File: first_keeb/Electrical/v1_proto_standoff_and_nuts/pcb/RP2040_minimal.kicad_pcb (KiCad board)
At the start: 4 copper layers, 67.1 x 66.8 mm, 68 parts, among them P1 USB-TYPE-C-016, Q1 SN74LV1T34DBV, SW1 SKRKAHE020, SW2 BUTT0, SW3 BUTT1, U1 NCP1117-3.3_SOT223, U2 MCP1525-TT, U3 PRTR5V0U2X, U4 MCP6004, U5 STM32F401RCTx, Y1 16MHz

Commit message: stm32 pcb almost done
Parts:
- removed the C1 at (115.5, 76.1)
- removed the C2 at (108.3, 80.8)
- removed the R3 at (80.3, 97.1)
- removed the R8 at (138.9, 103.1)
- removed the U4 at (105.1, 91.9)
- added C11: 10u, Capacitor_SMD:C_1206_3216Metric, F.Cu at (106.9, 112.4)
- added C12: 10u, Capacitor_SMD:C_1206_3216Metric, F.Cu at (109.8, 107.8)
- added C13: 100n, Capacitor_SMD:C_0402_1005Metric, F.Cu at (83.7, 85.5)
- added C6: 100n, Capacitor_SMD:C_0402_1005Metric, F.Cu at (97.6, 81.0)
- added D1: 1N4148WS, Diode_SMD:D_SOD-323, F.Cu at (102.1, 82.4)
- added FB1: GZ2012D601TF, Capacitor_SMD:C_0805_2012Metric, F.Cu at (80.5, 88.4)
- added J1: Conn_01x04_Socket, Connector_PinSocket_2.54mm:PinSocket_1x04_P2.54mm_Vertical, F.Cu at (85.3, 76.1)
- added J2: Conn_01x04_Socket, Connector_PinSocket_2.54mm:PinSocket_1x04_P2.54mm_Vertical, F.Cu at (84.3, 72.5)
- added R11: DNP, Resistor_SMD:R_0402_1005Metric, F.Cu at (113.9, 96.4)
- added R12: 0, Resistor_SMD:R_0402_1005Metric, F.Cu at (142.9, 101.4)
- added R13: 0, Resistor_SMD:R_0402_1005Metric, F.Cu at (142.9, 103.4)
- added R4: DNP, Capacitor_SMD:C_0603_1608Metric, F.Cu at (135.9, 87.5)
- added R6: DNP, Resistor_SMD:R_0402_1005Metric, F.Cu at (142.9, 95.4)
- added SW2: SKRKAHE020, Button_Switch_SMD:SW_Push_SPST_NO_Alps_SKRK, B.Cu at (89.5, 83.5)
- added SW4: BUTT3, Button_Switch_SMD:SW_Push_1P1T_NO_6x6mm_H9.5mm, B.Cu at (112.0, 120.0)
- added U5: MCP6001-OT, Package_TO_SOT_SMD:SOT-23-5, F.Cu at (146.9, 96.6)
- added U6: MCP6001-OT, Package_TO_SOT_SMD:SOT-23-5, F.Cu at (110.4, 94.0)
- C10: value 1u -> 10u; footprint Capacitor_SMD:C_0402_1005Metric -> Capacitor_SMD:C_1206_3216Metric
- C9: value 100n -> 10u; footprint Capacitor_SMD:C_0402_1005Metric -> Capacitor_SMD:C_1206_3216Metric
- R10, R7: value 0 -> DNP; footprint Capacitor_SMD:C_0603_1608Metric -> Resistor_SMD:R_0402_1005Metric
- R3: renamed from R6; moved to B.Cu
- R5: value 0 -> 10k; footprint Capacitor_SMD:C_0603_1608Metric -> Resistor_SMD:R_0402_1005Metric
- R9: value 0 -> DNP
- SW1: moved to B.Cu
- SW3: renamed from SW2; value BUTT0 -> BUTT1
- SW5: renamed from SW3; value BUTT1 -> BUTT2
- U1: value NCP1117-3.3_SOT223 -> AMS1117-2.5
- U2: value MCP1525-TT -> ME6208A44M3G
- moved D4 66.9 mm to (136.5, 77.5)
- moved C22 66.8 mm to (138.6, 77.8), turned to 90 degrees
- moved R5 41.1 mm to (98.7, 90.0), turned to 90 degrees
- moved C21 38.9 mm to (70.4, 61.0)
- moved D3 38.9 mm to (68.2, 61.0)
- moved U2 36.5 mm to (110.1, 110.9), turned to 180 degrees
- moved D2 32.9 mm to (100.6, 85.8), turned to 180 degrees
- moved C20 31.0 mm to (98.5, 85.7), turned to -90 degrees
- moved Q1 30.9 mm to (101.0, 85.8), turned to 0 degrees
- moved C10 28.6 mm to (107.9, 80.8)
- moved R9 28.2 mm to (114.2, 93.0)
- moved R10 26.1 mm to (115.8, 96.0), turned to -90 degrees
- moved U8 19.5 mm to (100.0, 100.0), turned to 180 degrees
- moved U9 19.5 mm to (119.5, 100.0)
- moved C18 18.3 mm to (120.9, 102.3), turned to 180 degrees
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- renumbered C3 to C1, C13 to C14, C14 to C15, C15 to C16, C16 to C17, C17 to C18, C18 to C19, C4 to C2, C19 to C20, C20 to C21, C21 to C22, C22 to C23, C23 to C24, C24 to C25, C25 to C26, C26 to C27, C27 to C28, C28 to C29, C5 to C3, C6 to C4, C7 to C5, C11 to C7, C12 to C8, D9 to D10, D10 to D11, D1 to D2, D2 to D3, D3 to D4, D4 to D5, D5 to D6, D6 to D7, D7 to D8, D8 to D9, R4 to R8, U5 to U4, U6 to U7, U7 to U9
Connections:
- C1 pad 1: +3V3 -> VDD
- C10 pad 1: ADC_VREF -> VDD
- C17 pad 2: +3V3 -> V_test
- C18 pad 2: +3V3 -> V_test
- C19 pad 2: +3V3 -> V_test
- C2 pad 1: +3V3 -> VDD
- C3 pad 1: +3V3 -> VDD
- C4 pad 1: +3V3 -> VDD
- C5 pad 1: +3V3 -> VDD
- C7 pad 1: ADC_VREF -> VDDA
- C8 pad 1: ADC_VREF -> VDDA
- C9 pad 1: GND -> +5V
- C9 pad 2: +3V3 -> GND
- Q1 pad 2: LED_D_5V -> LED_D
- Q1 pad 5: +5V -> Net-(D1-K)
- R10 pad 1: A_OUT2 -> Net-(U6-+)
- R10 pad 2: ADC_IN2 -> ALT_ADC_3
- R5 pad 1: A_OUT2 -> GND
- R5 pad 2: Net-(U4B-+) -> BOOT1
- R7 pad 1: A_OUT3 -> ADC_IN2
- R9 pad 1: A_OUT1 -> Net-(U6-V+)
- R9 pad 2: ADC_IN1 -> V_test
- SW1 pad 2: +3V3 -> VDD
- SW3 pad 1: unconnected-(SW2-Pad1) -> BUTT0
- SW5 pad 1: unconnected-(SW3-Pad1) -> BUTT1
- U1 pad 2: +3V3 -> VDD
- U2 pad 1: +3V3 -> GND
- U2 pad 2: ADC_VREF -> V_test
- U2 pad 3: GND -> +5V
- U4 pad 1: +3V3 -> VDD
- U4 pad 13: ADC_VREF -> VDDA
- U4 pad 15: unconnected-(U5-PA1-Pad15) -> BUTT0
- U4 pad 16: unconnected-(U5-PA2-Pad16) -> BUTT1
- U4 pad 17: unconnected-(U5-PA3-Pad17) -> BUTT2
- U4 pad 19: +3V3 -> VDD
- U4 pad 22: ALT_ADC_IN1 -> unconnected-(U4-PA6-Pad22)
- U4 pad 23: ALT_ADC_IN2 -> ADC_IN1
- U4 pad 24: ALT_ADC_IN3 -> ADC_IN2
- U4 pad 25: ADC_IN1 -> ADC_IN3
- U4 pad 26: ADC_IN2 -> unconnected-(U4-PB0-Pad26)
- U4 pad 27: ADC_IN3 -> unconnected-(U4-PB1-Pad27)
- U4 pad 28: unconnected-(U5-PB2-Pad28) -> BOOT1
- U4 pad 32: +3V3 -> VDD
- U4 pad 40: unconnected-(U5-PC9-Pad40) -> LED_D
- U4 pad 46: unconnected-(U5-PA13-Pad46) -> SWDIO
- U4 pad 48: +3V3 -> VDD
- U4 pad 49: unconnected-(U5-PA14-Pad49) -> SWCLK
- U4 pad 55: unconnected-(U5-PB3-Pad55) -> SWO
- U4 pad 58: unconnected-(U5-PB6-Pad58) -> USART1_TX
- U4 pad 59: unconnected-(U5-PB7-Pad59) -> USART1_RX
- U4 pad 64: +3V3 -> VDD
- U7 pad 1: +3V3 -> V_test
- U7 pad 3: A_OUT1 -> ADC_IN1
- U8 pad 1: +3V3 -> V_test
- U8 pad 3: A_OUT2 -> ALT_ADC_2
- U9 pad 1: +3V3 -> V_test
- U9 pad 3: A_OUT3 -> ALT_ADC_3
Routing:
- net V_test: track 0.00 -> 86.6 mm
- net BUTT2: track 0.00 -> 71.9 mm, vias 0 -> 1
- net BUTT1: track 0.00 -> 60.9 mm, vias 0 -> 1
- net BUTT0: track 0.00 -> 51.1 mm, vias 0 -> 1
- net VDD: track 0.00 -> 33.2 mm, vias 0 -> 15
- net +3V3: track 32.6 -> 0.00 mm, vias 15 -> 0
- net GND: track 81.6 -> 111.4 mm, vias 55 -> 179
- net ADC_IN3: track 0.00 -> 29.2 mm
- net +5V: track 16.2 -> 43.9 mm, vias 0 -> 1
- net Net-(D5-DOUT): track 25.0 -> 1.26 mm
- net Net-(D6-DOUT): track 21.3 -> 0.00 mm
- net Net-(D7-DOUT): track 20.9 -> 0.00 mm
- net SWDIO: track 0.00 -> 17.0 mm
- net NRST: track 0.00 -> 16.3 mm, vias 0 -> 2
- net ADC_IN2: track 0.00 -> 15.8 mm
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- added copper zone on B.Cu, net GND
- added copper zone on F.Cu, net GND
- added copper zone on In2.Cu, net GND
- added copper zone on B.Cu, net VDD
- removed copper zone on In2.Cu, net +3V3

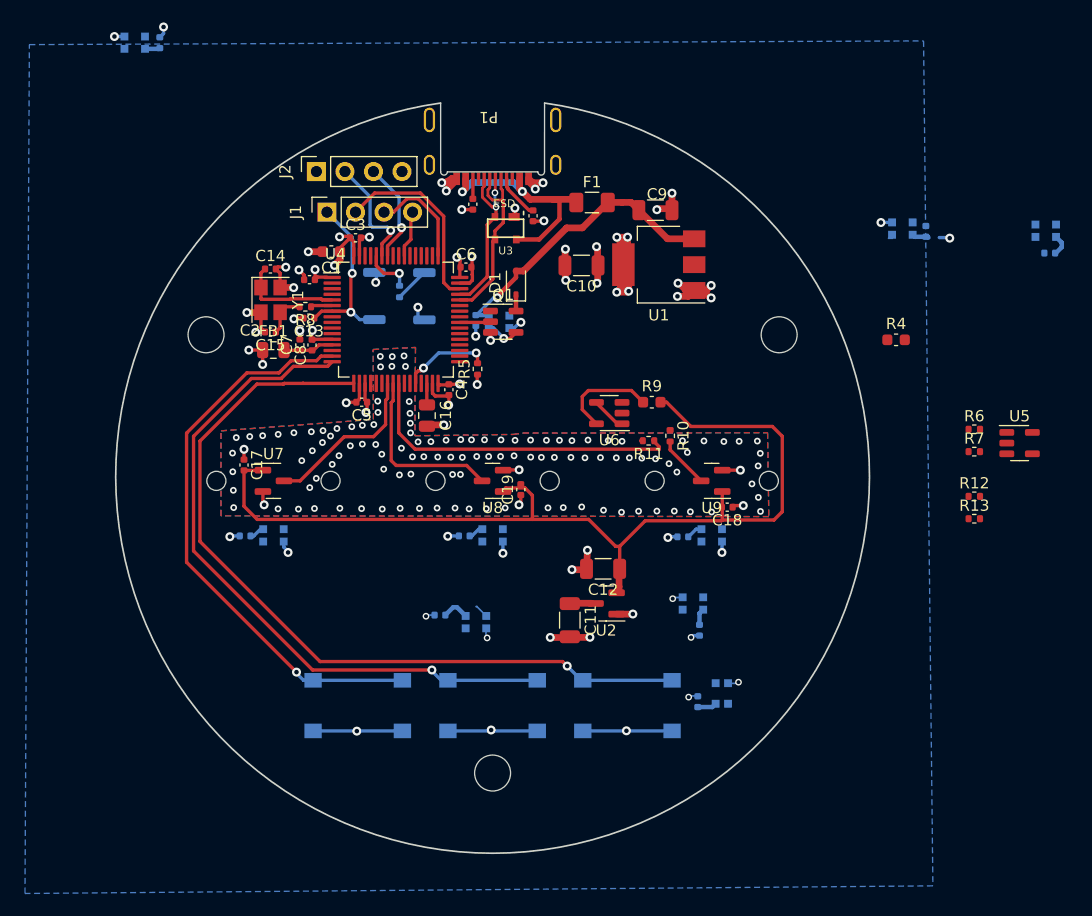
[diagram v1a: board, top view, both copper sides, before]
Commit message: vcc pour and ground
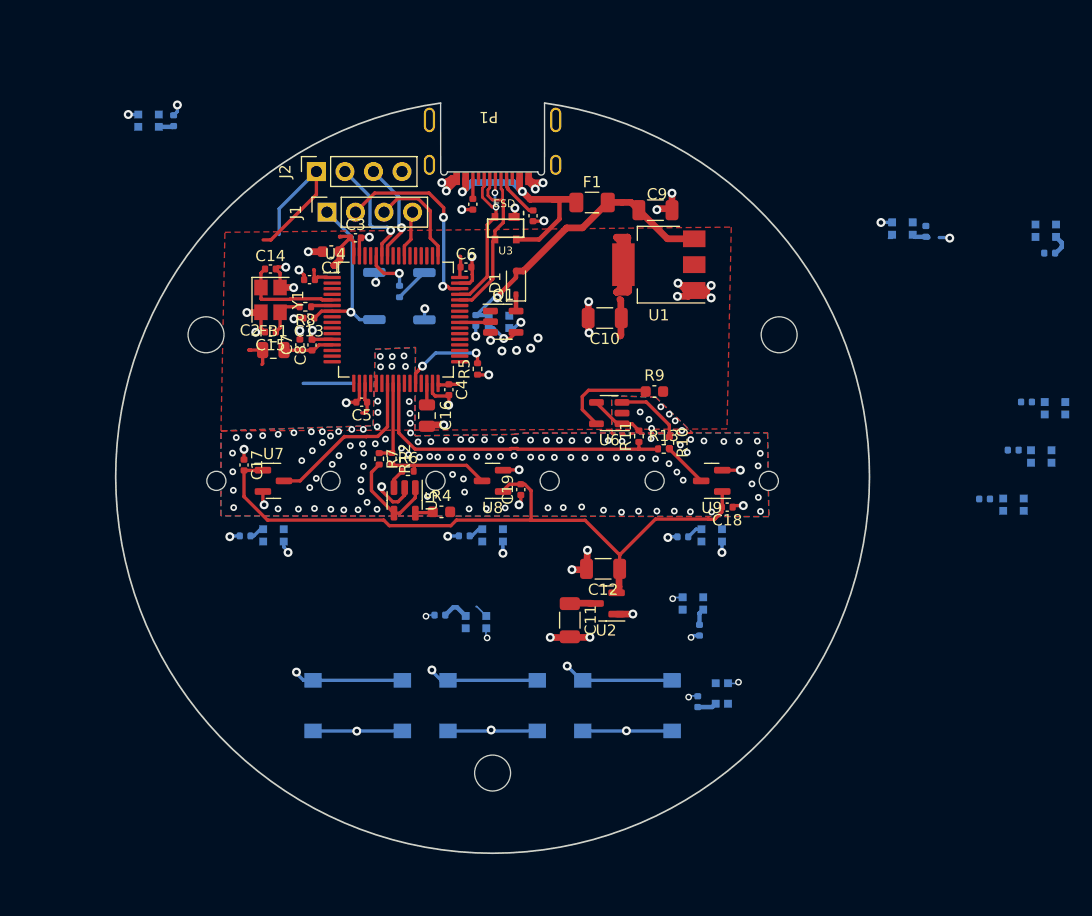
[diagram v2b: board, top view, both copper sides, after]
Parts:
- added C30: 100n, Capacitor_SMD:C_0402_1005Metric, B.Cu at (147.5, 93.0)
- added C31: 100n, Capacitor_SMD:C_0402_1005Metric, B.Cu at (146.3, 97.3)
- added C32: 100n, Capacitor_SMD:C_0402_1005Metric, B.Cu at (143.8, 101.6)
- added D12: WS2812B-2020, LED_SMD:LED_WS2812B-2020_PLCC4_2.0x2.0mm, B.Cu at (150.1, 93.5)
- added D13: WS2812B-2020, LED_SMD:LED_WS2812B-2020_PLCC4_2.0x2.0mm, B.Cu at (148.8, 97.8)
- added D14: WS2812B-2020, LED_SMD:LED_WS2812B-2020_PLCC4_2.0x2.0mm, B.Cu at (146.3, 102.1)
- moved U5 55.0 mm to (92.2, 101.7), turned to -90 degrees
- moved R7 53.0 mm to (89.9, 98.0), turned to -90 degrees
- moved R12 51.9 mm to (91.0, 98.0), turned to -90 degrees
- moved R6 50.5 mm to (92.5, 99.1)
- moved R4 43.3 mm to (95.5, 102.8)
- moved R13 28.3 mm to (115.2, 97.2)
- moved D3 7.05 mm to (69.4, 68.0)
- moved C21 7.05 mm to (71.6, 68.0)
- moved C10 5.12 mm to (110.0, 85.5)
- moved R9 0.98 mm to (114.4, 92.0)
- moved R11 0.95 mm to (113.0, 96.0), turned to 90 degrees
- moved R10 0.61 mm to (115.7, 96.6)
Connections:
- C12 pad 1: V_test -> +4V4
- C17 pad 2: V_test -> +4V4
- C18 pad 2: V_test -> +4V4
- C19 pad 2: V_test -> +4V4
- U2 pad 2: V_test -> +4V4
- U5 pad 1: Net-(U5--) -> O_ADC_IN2
- U5 pad 3: Net-(U5-+) -> ALT_ADC_2
- U5 pad 4: Net-(U5--) -> O_ADC_IN2
- U5 pad 5: Net-(U5-V+) -> V_test
- U6 pad 1: Net-(U6--) -> O_ADC_IN3
- U6 pad 3: Net-(U6-+) -> ALT_ADC_3
- U6 pad 4: Net-(U6--) -> O_ADC_IN3
- U6 pad 5: Net-(U6-V+) -> V_test
- U7 pad 1: V_test -> +4V4
- U8 pad 1: V_test -> +4V4
- U8 pad 3: ALT_ADC_2 -> S_ADC_IN2
- U9 pad 1: V_test -> +4V4
- U9 pad 3: ALT_ADC_3 -> S_ADC_IN3
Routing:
- net V_test: track 86.6 -> 0.00 mm
- net +4V4: track 0.00 -> 62.0 mm
- net BUTT2: track 71.9 -> 14.3 mm
- net BUTT1: track 60.9 -> 10.00 mm
- net BUTT0: track 51.1 -> 9.96 mm
- net VDD: track 33.2 -> 48.8 mm, vias 15 -> 1
- net Net-(U5--): track 0.00 -> 9.23 mm
- net ALT_ADC_2: track 0.00 -> 9.18 mm
- net ADC_IN2: track 15.8 -> 7.44 mm
- net Net-(U6-+): track 0.00 -> 6.14 mm
- net GND: track 111.4 -> 115.5 mm, vias 179 -> 196
- net Net-(U5-+): track 0.00 -> 1.76 mm
- net Net-(U5-V+): track 0.00 -> 1.50 mm
- net Net-(U6--): track 3.43 -> 4.84 mm
- net SWDIO: track 17.0 -> 17.8 mm, vias 0 -> 2
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- added copper zone on F.Cu, net VDD
- removed copper zone on B.Cu, net VDD

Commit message: adds leds
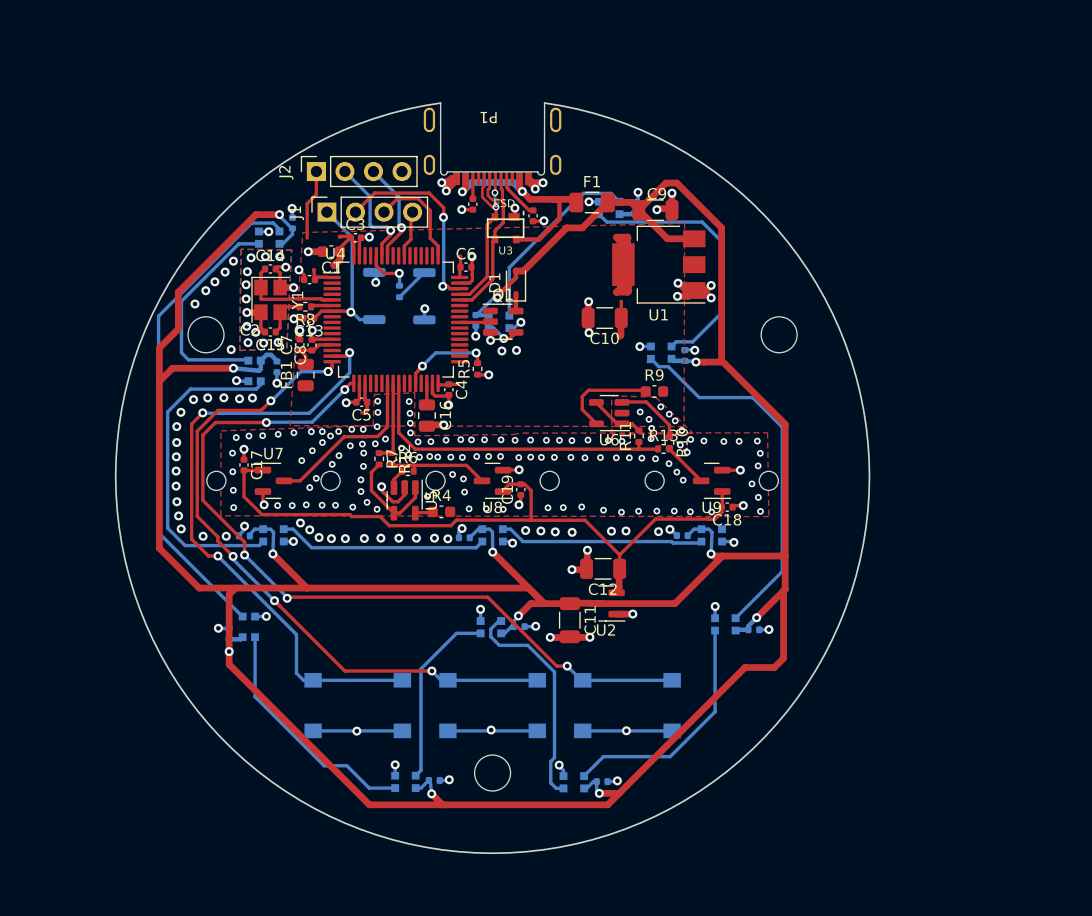
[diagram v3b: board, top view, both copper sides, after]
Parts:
- moved D11 71.5 mm to (78.8, 90.2), turned to 90 degrees
- moved C30 70.6 mm to (77.9, 104.9)
- moved D12 70.5 mm to (80.5, 104.8)
- moved C29 69.5 mm to (80.8, 89.9), turned to -90 degrees
- moved C28 51.2 mm to (82.2, 77.1), turned to 90 degrees
- moved D10 49.8 mm to (80.1, 78.4)
- moved C31 49.5 mm to (97.5, 105.1)
- moved D13 49.3 mm to (100.0, 104.8)
- moved D9 42.5 mm to (78.3, 113.0)
- moved C27 42.1 mm to (76.5, 113.6)
- moved C21 41.7 mm to (112.6, 75.7)
- moved D3 41.7 mm to (110.4, 75.7)
- moved C24 38.6 mm to (109.7, 126.8), turned to 0 degrees
- moved D8 35.0 mm to (92.2, 126.8), turned to 0 degrees
- moved D6 34.6 mm to (107.2, 126.8), turned to 0 degrees
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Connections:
- D11 pad 1: unconnected-(D11-DOUT-Pad1) -> Net-(D11-DOUT)
- D12 pad 3: unconnected-(D12-DIN-Pad3) -> Net-(D11-DOUT)
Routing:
- net +5V: track 43.9 -> 310.5 mm, vias 1 -> 12
- net BUTT2: track 14.3 -> 70.7 mm, vias 1 -> 5
- net BUTT1: track 10.00 -> 60.3 mm, vias 1 -> 6
- net BUTT0: track 9.96 -> 55.9 mm, vias 1 -> 3
- net Net-(D10-DIN): track 0.00 -> 44.5 mm
- net Net-(D4-DOUT): track 0.36 -> 33.3 mm
- net Net-(D11-DOUT): track 0.00 -> 29.2 mm
- net Net-(D3-DOUT): track 0.00 -> 24.0 mm
- net Net-(D8-DOUT): track 0.00 -> 21.1 mm
- net Net-(D6-DOUT): track 0.00 -> 20.2 mm
- net Net-(D5-DOUT): track 1.26 -> 21.3 mm
- net Net-(D10-DOUT): track 0.00 -> 19.8 mm
- net Net-(D12-DOUT): track 0.00 -> 18.6 mm
- net Net-(D13-DOUT): track 0.00 -> 18.2 mm
- net Net-(D2-DOUT): track 0.00 -> 17.1 mm
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
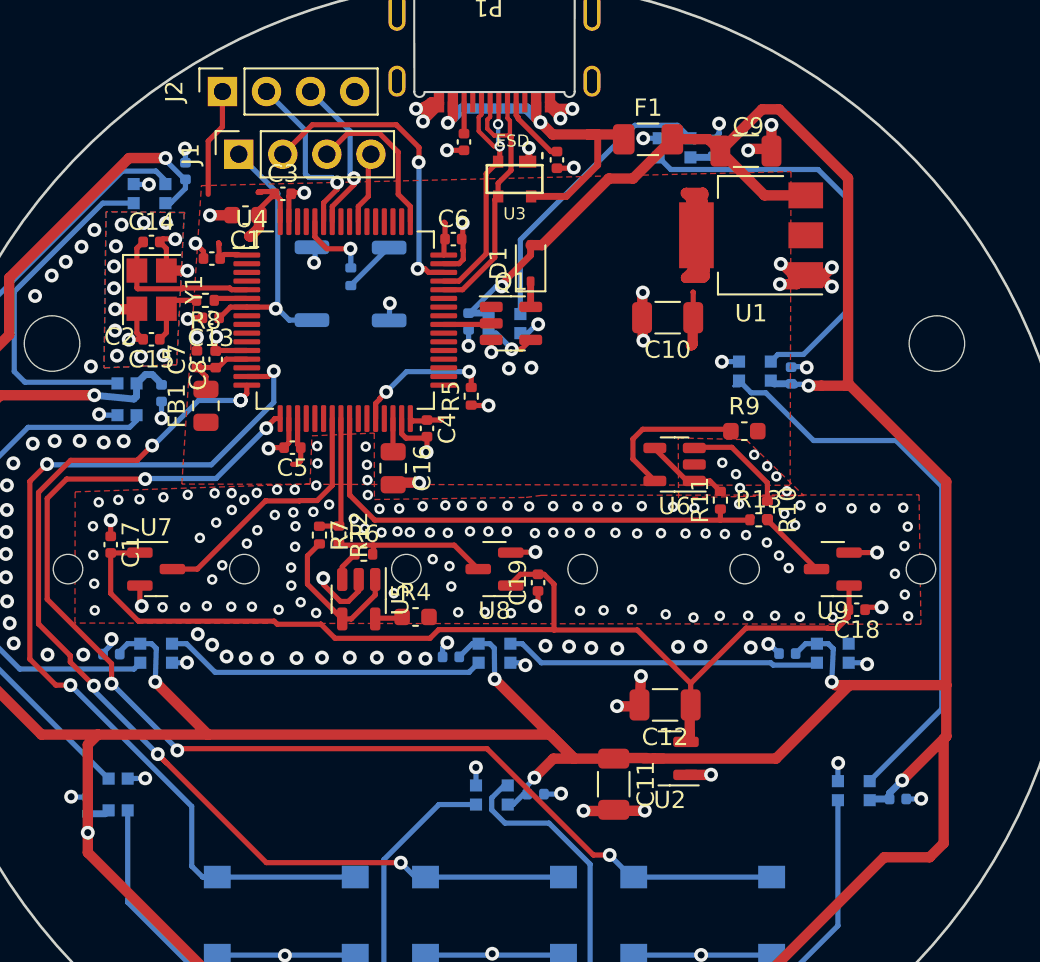
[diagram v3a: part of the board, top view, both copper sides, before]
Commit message: create vdd traces instead of pour
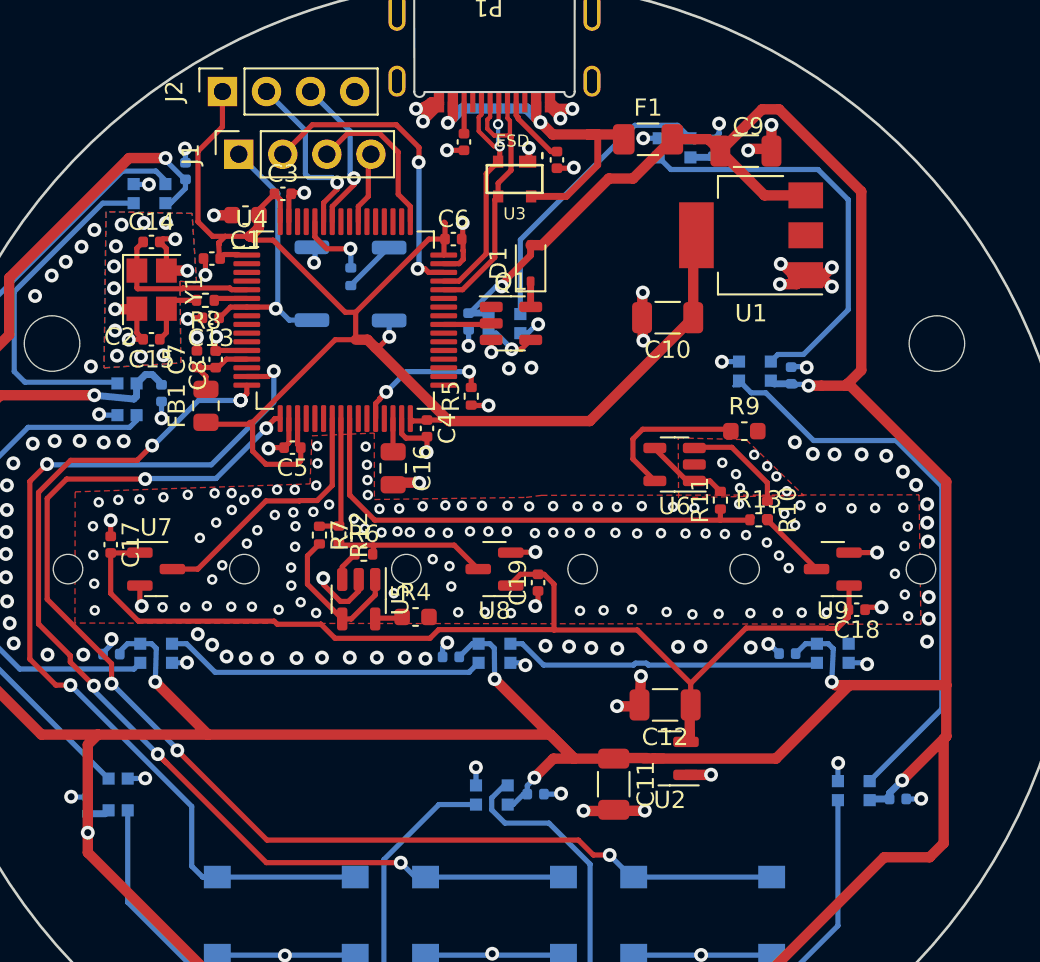
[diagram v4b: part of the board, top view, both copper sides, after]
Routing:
- net VDD: track 36.5 -> 88.8 mm
- net +5V: track 310.5 -> 311.2 mm
- net GND: track 124.7 -> 124.4 mm, vias 246 -> 259
- removed copper zone on F.Cu, net VDD
